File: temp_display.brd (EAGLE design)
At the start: 101.6 x 76.2 mm, 65 parts, among them IC2 ATMEGA168PROUND, Q1 2N2907

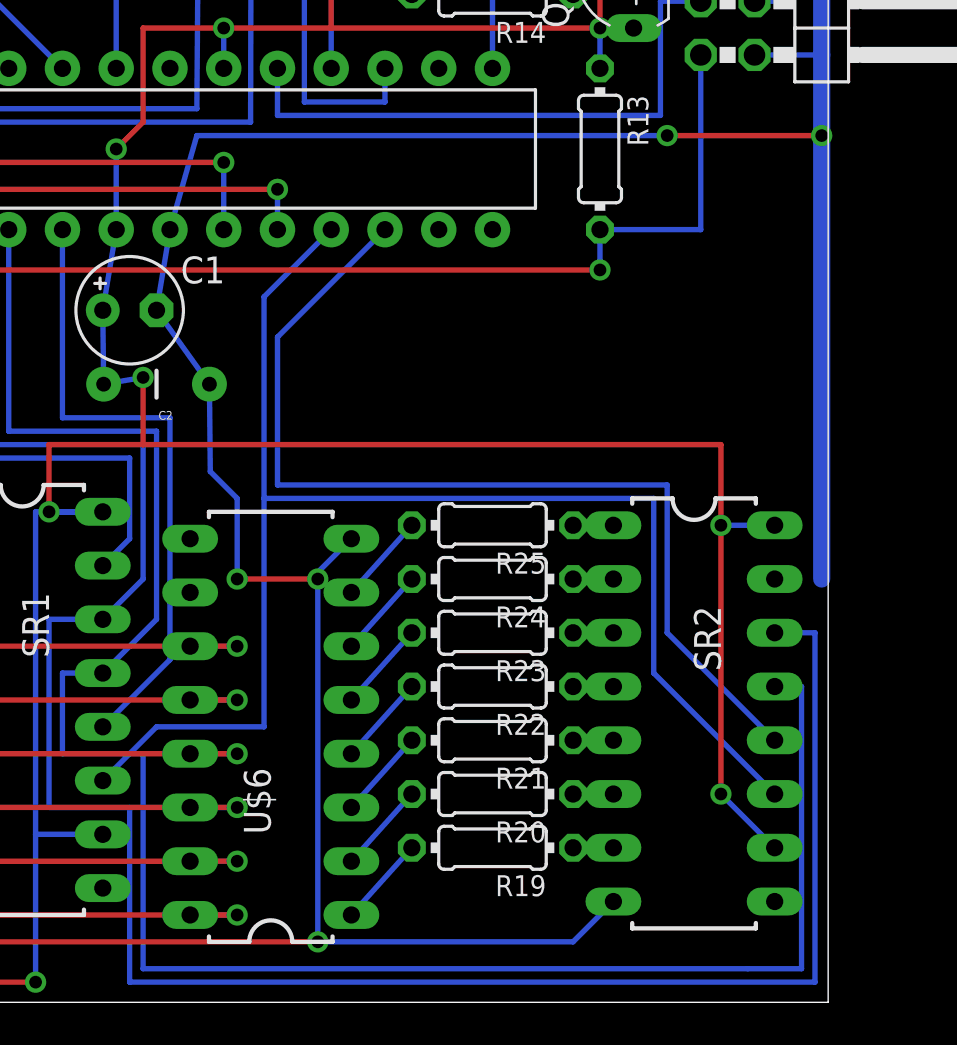
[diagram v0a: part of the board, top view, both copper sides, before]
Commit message: Removed resistors from ULN2003 darlington array
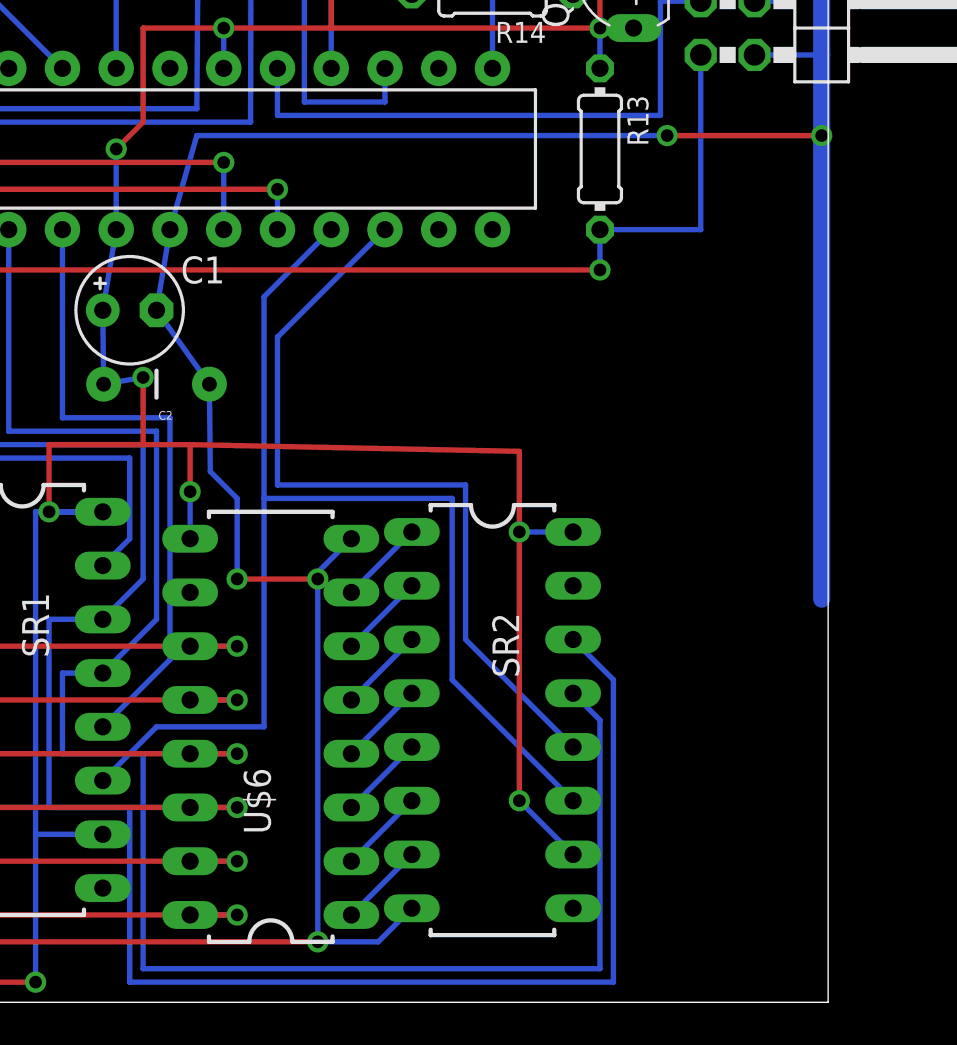
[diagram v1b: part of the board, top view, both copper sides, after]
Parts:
- removed R19, R20, R21, R22, R23, R24, R25: (no value), resistor:0204/7
- moved SR2 9.53 mm to (85.7, 13.0)
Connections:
- net N$10 renamed K_L7S_2
- net N$11 renamed K_L7S_1
- net N$13 renamed K_IL34
- net N$14 renamed K_IL12
- net N$59 renamed K_IL56
- net N$60 renamed STCP2
- net N$9 renamed K_L7S_3
- removed net N$16: R19.2, U$6.1
- removed net N$28: R20.2, U$6.2
- removed net N$29: R21.2, U$6.3
- removed net N$32: R22.2, U$6.4
- removed net N$45: R23.2, U$6.5
- removed net N$47: R24.2, U$6.6
- removed net N$49: R25.2, U$6.7
- net N$50: now also U$6.7; no longer R25.1
- net N$53: now also U$6.6; no longer R24.1
- net N$54: now also U$6.5; no longer R23.1
- net N$55: now also U$6.4; no longer R22.1
- net N$56: now also U$6.3; no longer R21.1
- net N$57: now also U$6.2; no longer R20.1
- net N$58: now also U$6.1; no longer R19.1
- net VCC: now also U$6.9
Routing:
- net DS: track 102.4 -> 91.4 mm
- net OE: track 94.4 -> 83.8 mm
- net STCP2: track 46.8 -> 37.5 mm
- net SHCP: track 68.2 -> 59.0 mm
- net GND: track 490.5 -> 481.8 mm
- net VCC: track 324.8 -> 319.7 mm, vias 10 -> 11
- net N$49: track 4.27 -> 0.00 mm
- net N$32: track 4.27 -> 0.00 mm
- net N$28: track 4.27 -> 0.00 mm
- net N$16: track 4.27 -> 0.00 mm
- net N$45: track 4.27 -> 0.00 mm
- net N$29: track 4.27 -> 0.00 mm
- net N$47: track 4.27 -> 0.00 mm
- net N$58: track 1.91 -> 4.04 mm
- net N$57: track 1.91 -> 4.04 mm
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
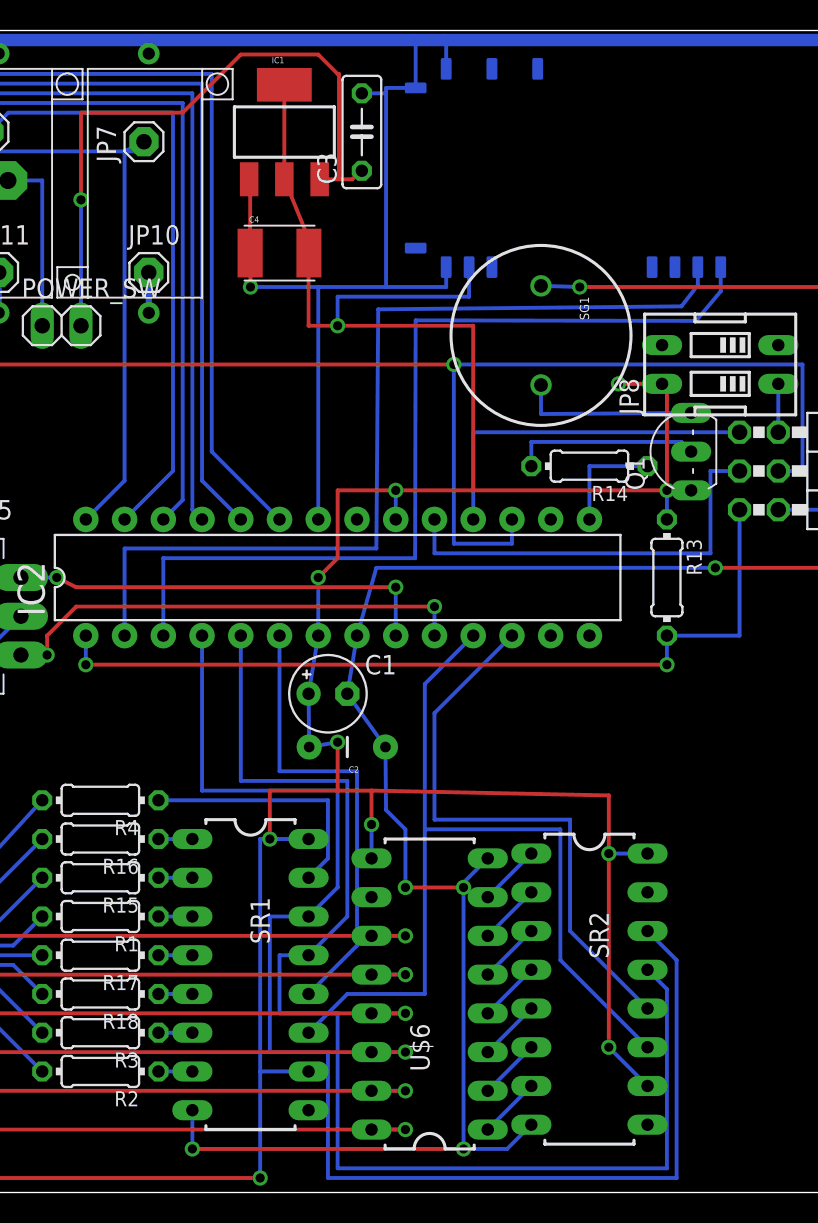
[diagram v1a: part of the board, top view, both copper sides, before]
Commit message: Connected 595 shift registers serially.
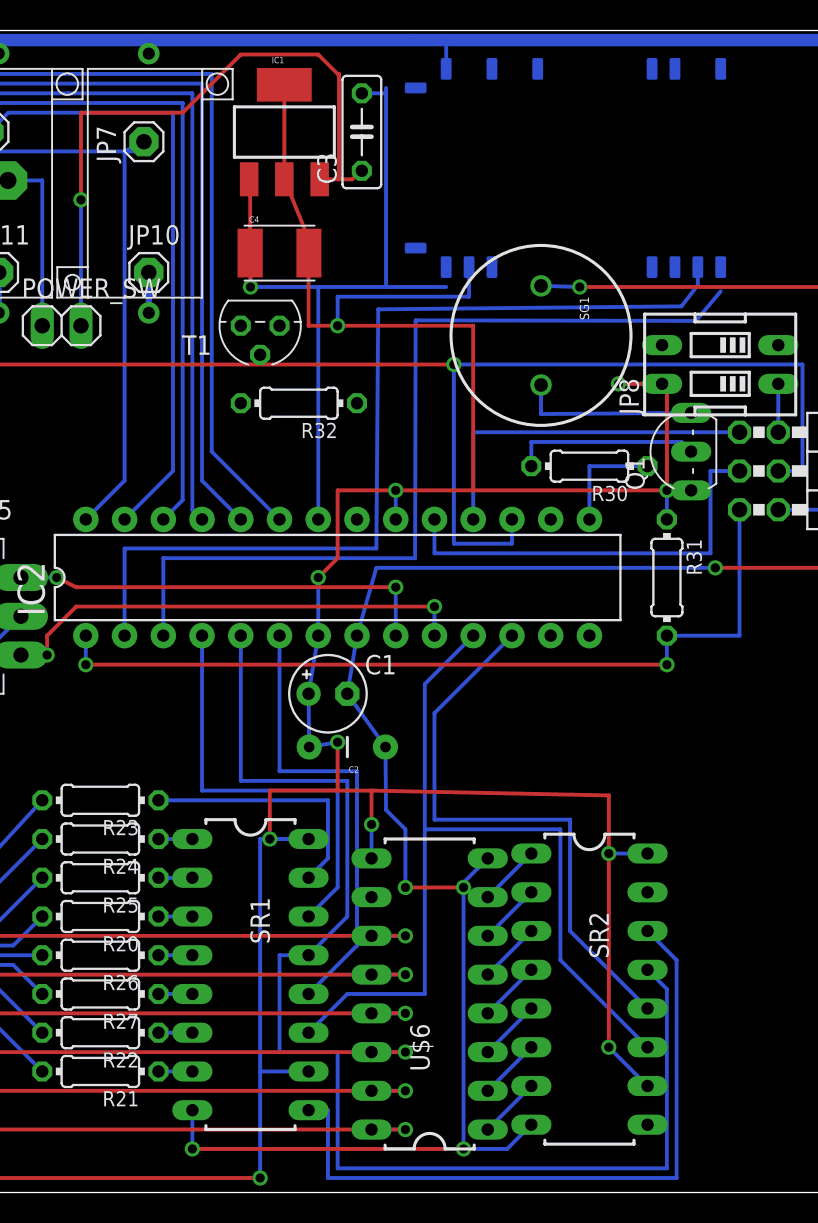
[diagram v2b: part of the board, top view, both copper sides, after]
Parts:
- removed R10, R7, R8, R9: R-USR_POWER-15X8.5, kirill:R_POWER-15X8.5
- added R20, R21, R22, R23: 147, resistor:0204/7
- added R32: (no value), resistor:0204/7
- added T1: BC547, transistor:TO92
- R1, R2, R3, R4: value (none) -> R-USR_POWER-15X8.5; device resistor:0204/7 -> kirill:R_POWER-15X8.5
- R24, R25, R26, R27: value (none) -> 147
- moved R2 69.0 mm to (17.5, 66.4), turned to 90 degrees
- moved R1 66.9 mm to (7.62, 66.4), turned to 90 degrees
- moved R3 62.1 mm to (27.3, 66.4), turned to 90 degrees
- moved R4 44.2 mm to (37.1, 66.4), turned to 90 degrees
- moved R5 39.4 mm to (47.0, 66.4)
- moved R6 39.4 mm to (56.8, 66.4)
- renumbered R13 to R31, R14 to R30, R15 to R25, R16 to R24, R17 to R26, R18 to R27
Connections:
- net N$20 renamed SERIAL_RX
- net N$46 renamed SERIAL_TX
- new net BTH_PW_TRANS: IC2.14, R32.1
- new net N$1: SR1.9, SR2.14
- new net N$2: R32.2, T1.2
- new net N$3: T1.3, U$1.13, U$1.21
- net DS: no longer SR2.14
- net GND: now also R1.P$2, R2.P$2, R3.P$2, R4.P$2, T1.1; no longer R10.P$2, R7.P$2, R8.P$2, R9.P$2, U$1.13, U$1.21
- net N$15: now also R20.1; no longer R1.1
- net N$23: now also R1.P$1; no longer R5.P$1
- net N$24: now also R2.P$1; no longer R6.P$1
- net N$26: now also R23.1; no longer R4.1
- net N$35: now also R3.P$1; no longer R7.P$1
- net N$36: now also R4.P$1; no longer R8.P$1
- net N$37: now also R5.P$1; no longer R9.P$1
- net N$38: now also R6.P$1; no longer R10.P$1
- net N$42: now also R21.1; no longer R2.1
- net N$44: now also R22.1; no longer R3.1
- net SEG_DP: now also R20.2; no longer R1.2
- net SEG_E: now also R23.2; no longer R4.2
- net SEG_F: now also R22.2; no longer R3.2
- net SEG_G: now also R21.2; no longer R2.2
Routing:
- net DS: track 91.4 -> 28.1 mm
- net N$1: track 0.00 -> 45.6 mm
- net GND: track 481.8 -> 475.5 mm
- net SERIAL_TX: track 59.7 -> 58.1 mm

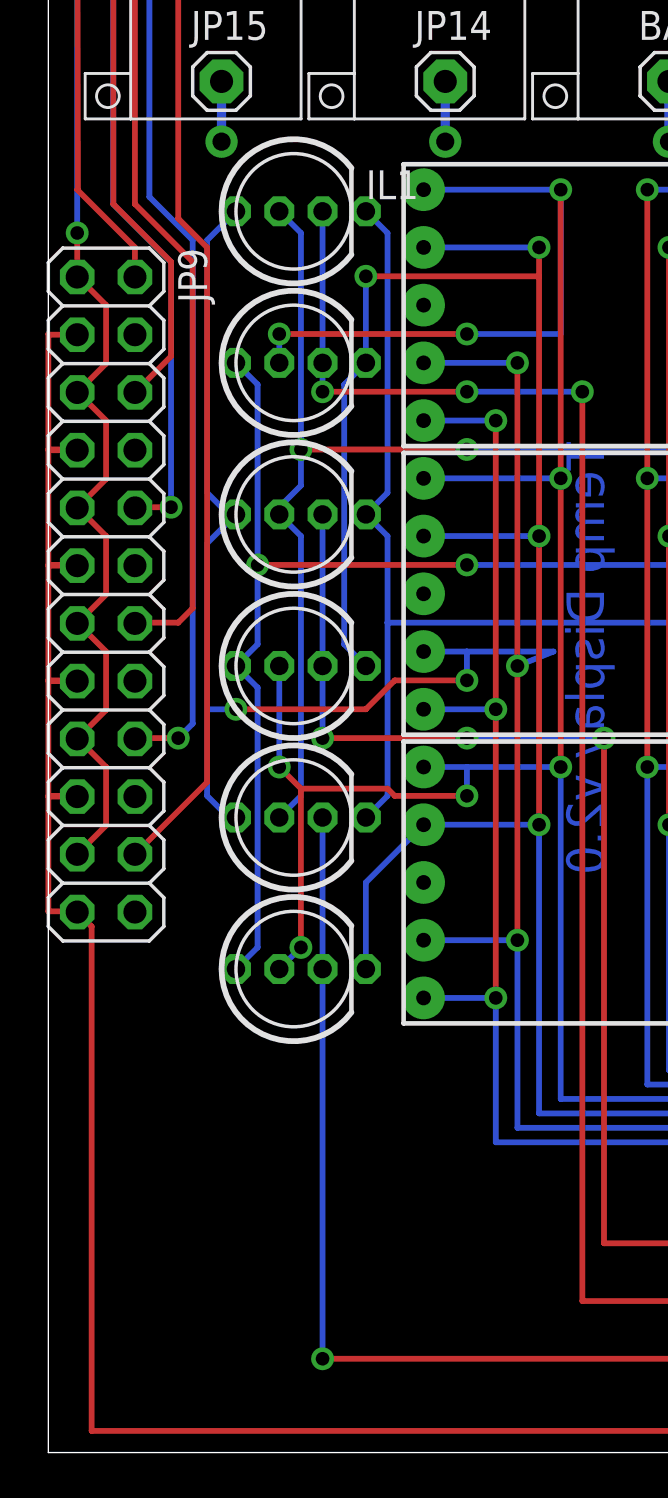
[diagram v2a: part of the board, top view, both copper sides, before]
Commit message: Intermediate version: working on the indicator LEDs
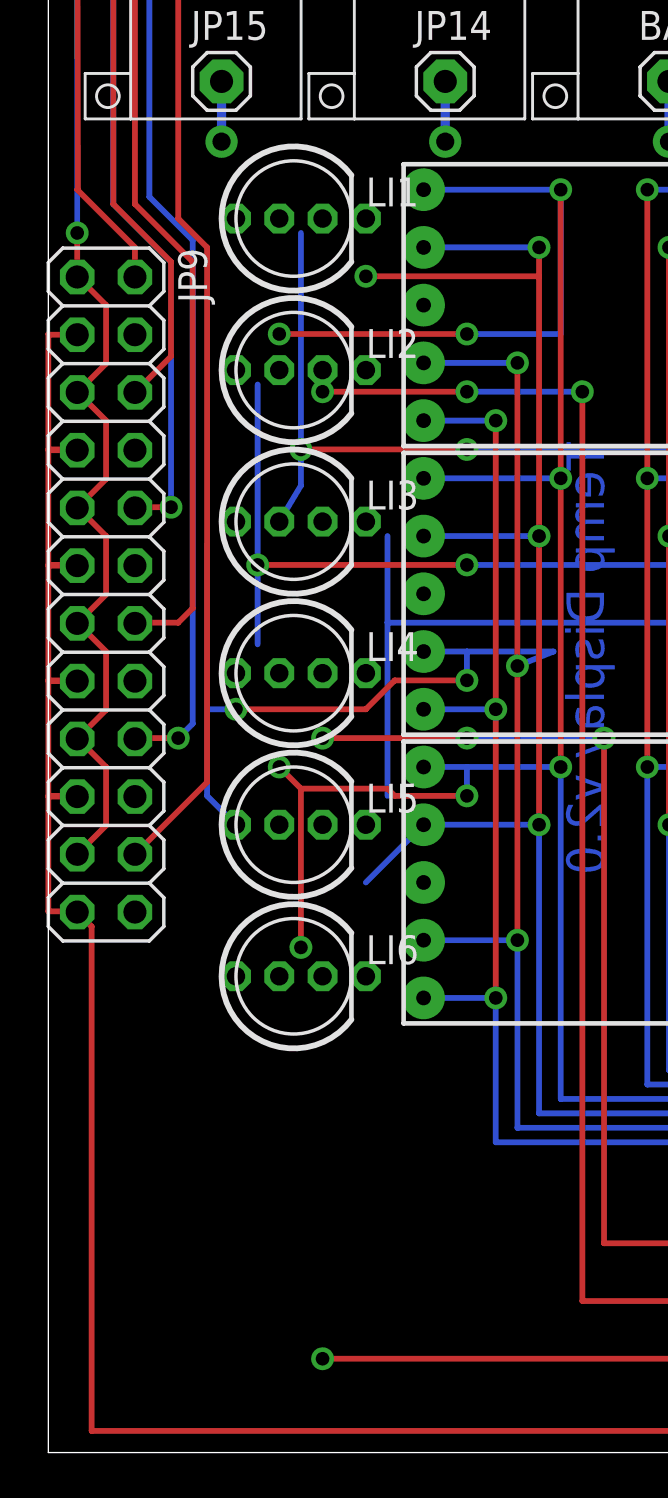
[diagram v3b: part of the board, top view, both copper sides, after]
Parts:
- removed IL1, IL2, IL3, IL4, IL5, IL6: LED_RGB_CC, kirill:LED_RGB_5MM_
- added LI1, LI2, LI3, LI4, LI5, LI6: (no value), kirill:LED_RGB_5MM_
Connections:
- removed net N$33: IC2.16, S1.1, S1.2
- net K_IL12: now also LI1.K, LI2.K; no longer IL1.K, IL2.K
- net K_IL34: now also LI3.K, LI4.K; no longer IL3.K, IL4.K
- net K_IL56: now also LI5.K, LI6.K; no longer IL5.K, IL6.K
- net N$27: now also S1.1, S1.2
- net SEG_A: now also LI2.A_R, LI4.A_R, LI6.A_R; no longer IL2.A_B, IL4.A_B, IL6.A_B
- net SEG_B: now also LI2.A_G, LI4.A_G, LI6.A_G; no longer IL2.A_G, IL4.A_G, IL6.A_G
- net SEG_C: now also LI2.A_B, LI4.A_B, LI6.A_B; no longer IL2.A_R, IL4.A_R, IL6.A_R
- net SEG_D: now also LI1.A_R, LI3.A_R, LI5.A_R; no longer IL1.A_B, IL3.A_B, IL5.A_B
- net SEG_E: now also LI1.A_G, LI3.A_G, LI5.A_G; no longer IL1.A_G, IL3.A_G, IL5.A_G
- net SEG_F: now also LI1.A_B, LI3.A_B, LI5.A_B; no longer IL1.A_R, IL3.A_R, IL5.A_R
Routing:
- net K_IL56: track 87.6 -> 63.8 mm
- net SEG_A: track 115.3 -> 93.6 mm
- net SEG_D: track 107.8 -> 90.9 mm
- net SEG_C: track 121.3 -> 104.4 mm
- net SEG_F: track 122.5 -> 105.8 mm
- net SEG_E: track 103.5 -> 88.2 mm
- net K_IL34: track 95.9 -> 86.0 mm
- net K_IL12: track 111.8 -> 103.8 mm
- net SEG_B: track 128.2 -> 121.2 mm

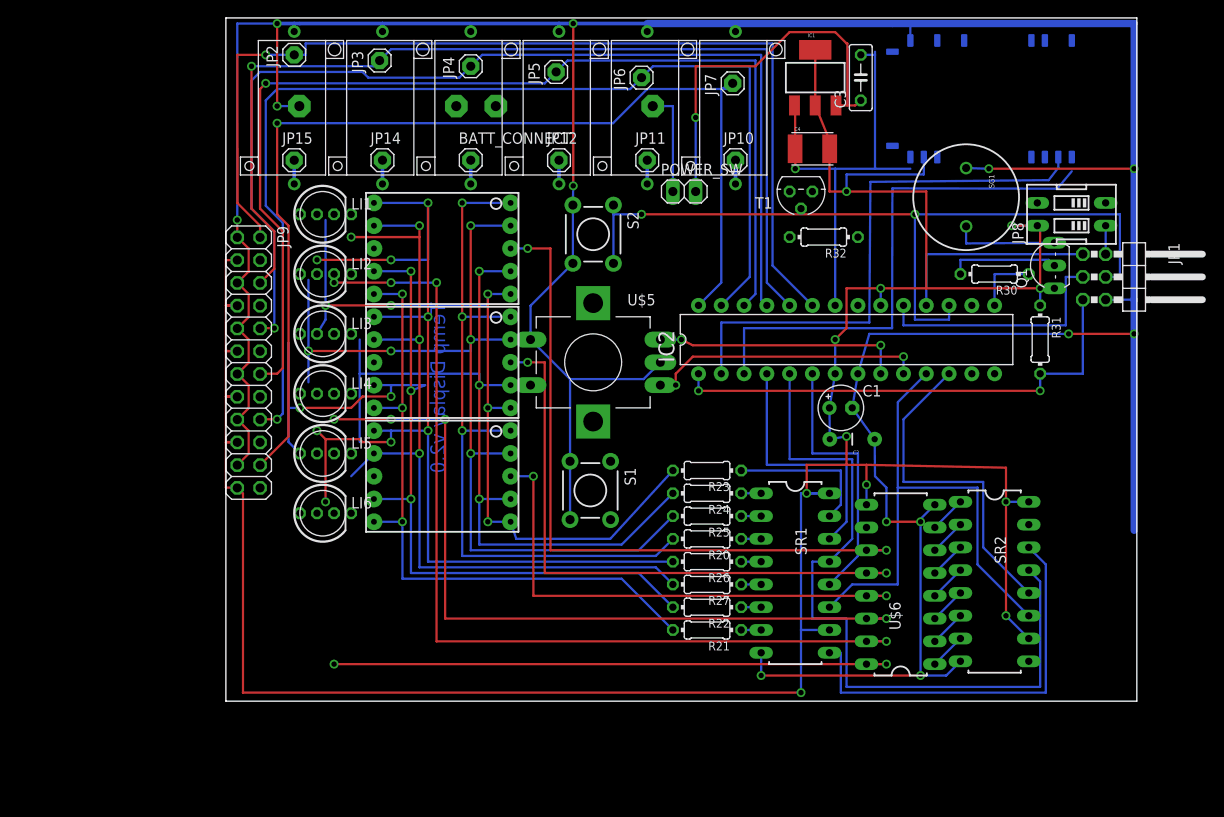
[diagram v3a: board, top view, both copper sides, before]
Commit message: 
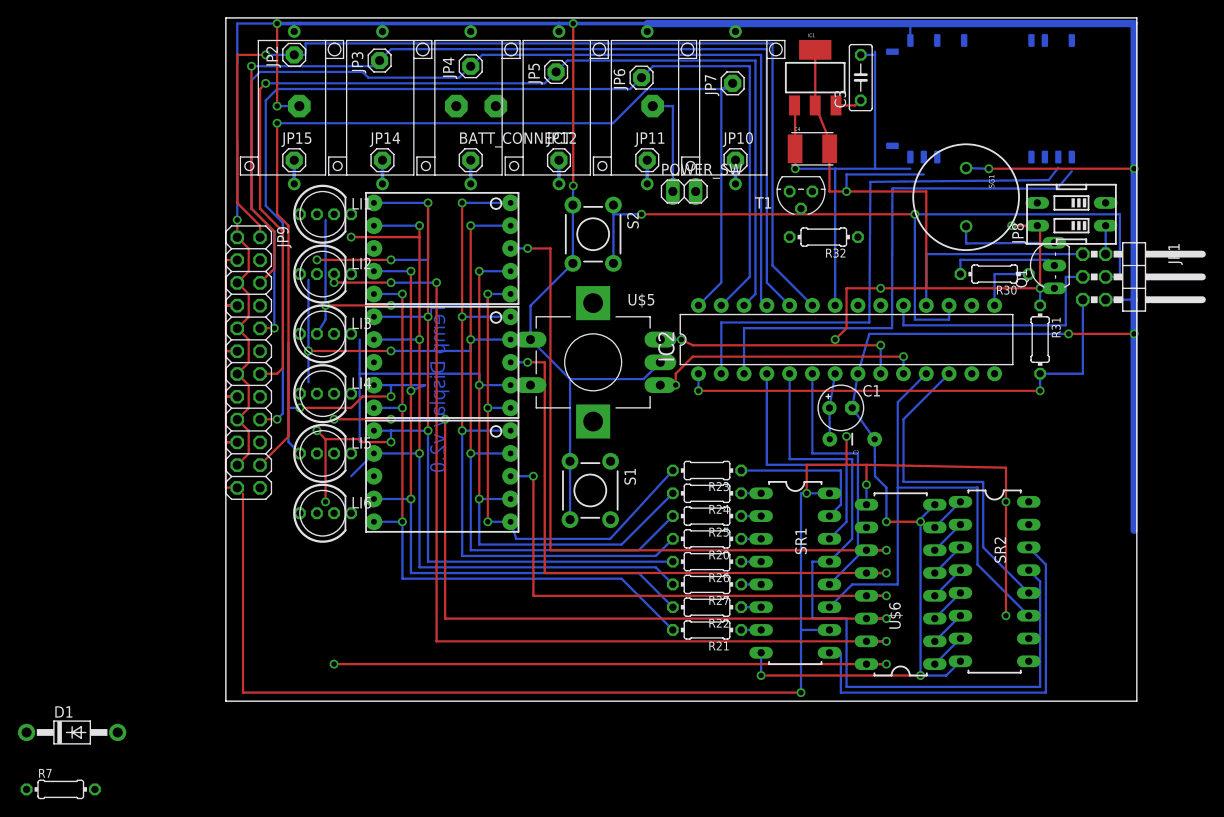
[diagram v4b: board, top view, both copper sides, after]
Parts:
- added D1: 1N4004, adafruit:DO41-10
- added R7: (no value), resistor:0204/7
- BAT1, BAT2: value BATTERY_CR2032 -> (none)
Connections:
- removed net N$39: C3.1, IC1.3, POWER_SW.2
- new net +3V3: C4.A, D1.C, IC1.2, IC1.4, U$1.12
- new net +5V: C1.+, C2.2, C3.1, IC1.3, IC2.20, IC2.7, JP8.4, JP9.11, JP9.15, JP9.19, JP9.23, JP9.3, JP9.7, POWER_SW.2, Q1.E, SR1.10, SR1.16, SR2.10, SR2.16, U$6.9
- new net N$4: D1.A, R7.2, U$1.2
- net SERIAL_RX: now also R7.1; no longer U$1.2
- net VCC: no longer C1.+, C2.2, C4.A, IC1.2, IC1.4, IC2.20, IC2.7, JP8.4, JP9.11, JP9.15, JP9.19, JP9.23, JP9.3, JP9.7, Q1.E, SR1.10, SR1.16, SR2.10, SR2.16, U$1.12, U$6.9
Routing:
- net VCC: track 319.7 -> 76.8 mm, vias 11 -> 5
- net +5V: track 0.00 -> 211.0 mm, vias 0 -> 6
- net N$39: track 42.9 -> 0.00 mm, vias 1 -> 0
- net +3V3: track 0.00 -> 11.3 mm
- net SERIAL_RX: track 60.7 -> 59.5 mm
